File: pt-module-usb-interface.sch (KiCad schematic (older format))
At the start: 9 parts, among them J8 USB_OTG, U7 FT230XS

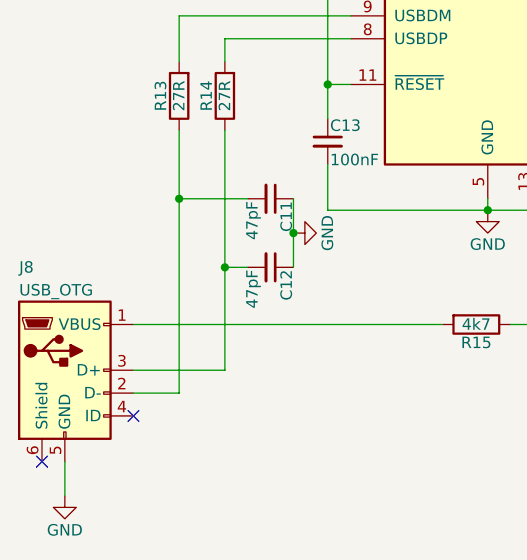
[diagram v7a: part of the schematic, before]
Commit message: Only 1 error in ERC check. It's in PWREN.
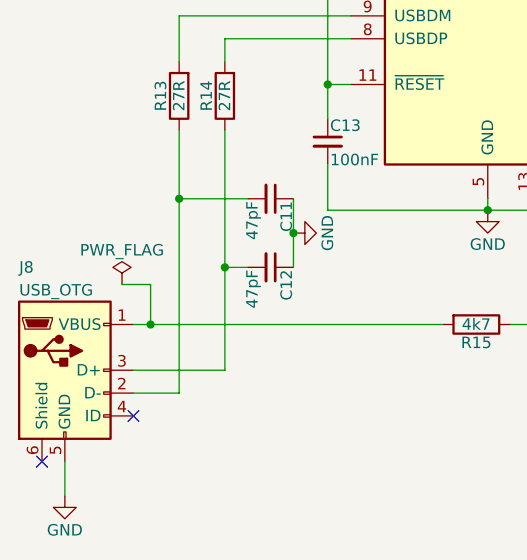
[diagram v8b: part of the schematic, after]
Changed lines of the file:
@@
 $EndComp
 $Comp
-L GND #PWR058
+L GND #PWR060
 U 1 1 59837539
 P 5900 4500
-F 0 "#PWR058" H 5900 4250 50  0001 C CNN
+F 0 "#PWR060" H 5900 4250 50  0001 C CNN
 F 1 "GND" H 5900 4350 50  0000 C CNN
 F 2 "" H 5900 4500 50  0001 C CNN
@@
 $EndComp
 $Comp
-L GND #PWR059
+L GND #PWR061
 U 1 1 59837659
 P 3800 4750
-F 0 "#PWR059" H 3800 4500 50  0001 C CNN
+F 0 "#PWR061" H 3800 4500 50  0001 C CNN
 F 1 "GND" H 3800 4600 50  0000 C CNN
 F 2 "" H 3800 4750 50  0001 C CNN
@@
 NoConn ~ 4100 4400
 $Comp
-L +3.3V #PWR060
+L +3.3V #PWR062
 U 1 1 59837A65
 P 5650 1750
-F 0 "#PWR060" H 5650 1600 50  0001 C CNN
+F 0 "#PWR062" H 5650 1600 50  0001 C CNN
 F 1 "+3.3V" H 5650 1890 50  0000 C CNN
 F 2 "" H 5650 1750 50  0001 C CNN
@@
 $EndComp
 $Comp
-L GND #PWR061
+L GND #PWR063
 U 1 1 59838D4F
 P 4800 3600
-F 0 "#PWR061" H 4800 3350 50  0001 C CNN
+F 0 "#PWR063" H 4800 3350 50  0001 C CNN
 F 1 "GND" H 4800 3450 50  0000 C CNN
 F 2 "" H 4800 3600 50  0001 C CNN
@@
 $EndComp
 $Comp
-L GND #PWR062
+L GND #PWR064
 U 1 1 59839F17
 P 5650 3500
-F 0 "#PWR062" H 5650 3250 50  0001 C CNN
+F 0 "#PWR064" H 5650 3250 50  0001 C CNN
 F 1 "GND" H 5650 3350 50  0000 C CNN
 F 2 "" H 5650 3500 50  0001 C CNN
@@
 NoConn ~ 3700 4600
 $Comp
-L PWR_FLAG #FLG063
+L PWR_FLAG #FLG065
 U 1 1 599577D8
 P 6300 4350
-F 0 "#FLG063" H 6300 4425 50  0001 C CNN
+F 0 "#FLG065" H 6300 4425 50  0001 C CNN
 F 1 "PWR_FLAG" H 6300 4500 50  0000 C CNN
 F 2 "" H 6300 4350 50  0001 C CNN
@@
 	6300 4425 5900 4425
 Connection ~ 5900 4425
+$Comp
+L PWR_FLAG #FLG?
+U 1 1 5996A652
+P 4050 3825
+F 0 "#FLG?" H 4050 3900 50  0001 C CNN
+F 1 "PWR_FLAG" H 4050 3975 50  0000 C CNN
+F 2 "" H 4050 3825 50  0001 C CNN
+F 3 "" H 4050 3825 50  0001 C CNN
+	1    4050 3825
+	1    0    0    -1
+$EndComp
+Wire Wire Line
+	4050 3825 4175 3825
+Wire Wire Line
+	4175 3825 4175 4000
+Connection ~ 4175 4000
 $EndSCHEMATC
